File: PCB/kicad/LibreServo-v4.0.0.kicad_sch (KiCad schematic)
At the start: 105 parts, among them J1 SLOT, J2 SLOT, J3 FFC-5, J4 FFC-5, J5 HEADER_4_1.27_0.3, J6 JST_PH-4_HOLEB, J7 JST_PH-4_HOLEB, M1 M1, M2 MOSFET_N+P, M3 MOSFET_N+P, M4 FAN3227/4, M5 FAN3227/4, U1 M0G3518QRHBRQ1, U10 AEAT-8800, U2 MPM3610, U3 AP2112, U4 ACS711, U5 ADM2587E, U6 ADM3055E, U7 OPTIGA_TRUST_M, Y1 OSCILATOR

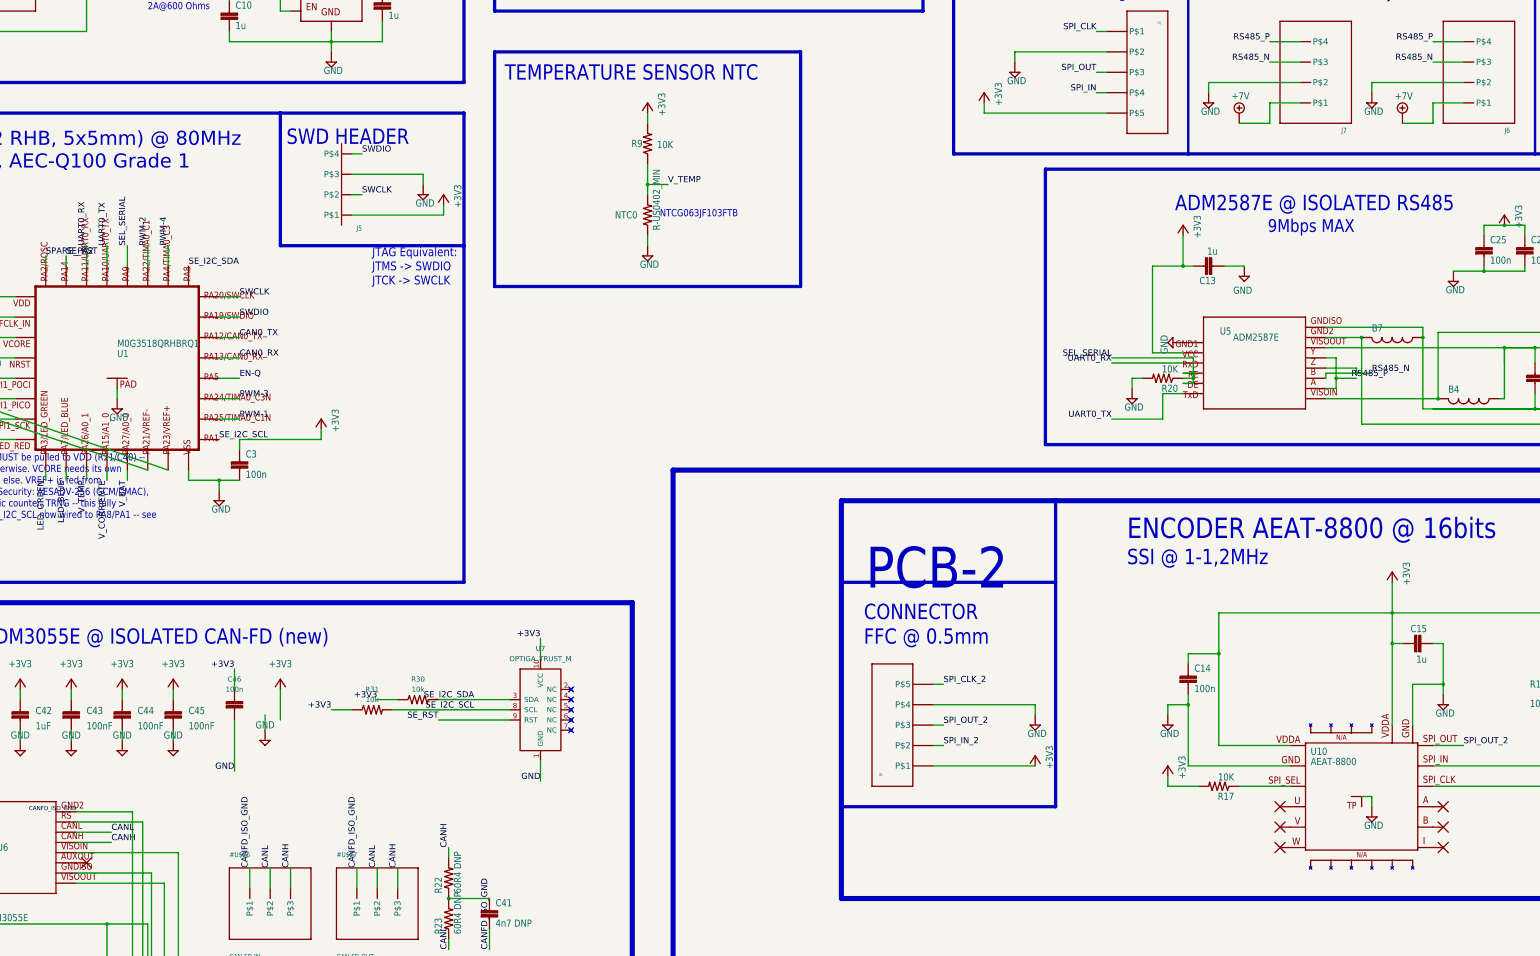
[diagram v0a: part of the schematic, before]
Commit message: fix(sch): add PWR_FLAG on 10 legitimately-external/isolated supply nets
Places power:PWR_FLAG instances on the nets ERC correctly reports as
"power_pin_not_driven" because nothing in the schematic supplies them
from a real driven output pin -- they're genuinely externally-sourced
or internally isoPower-generated:

  - U5 (ADM2587E) GNDISO / GND2 / VISOIN / VISOOUT -- isolated-side
    supply generated by the part's own integrated isoPower converter,
    not modeled as a driving pin on the symbol.
  - U6 (ADM3055E) the same 4 isolated-side nets, mirroring U5.
  - Board +7V and GND, sourced from the external battery/motor
    connector (J6/J7), which this schematic correctly can't infer as
    "driven" without an explicit flag.

Also registers the "power" library in the project's own sym-lib-table
(previously only resolvable via the user's global KiCad config) and
adds the ki_keywords property that was missing from the first,
incomplete embed -- both were needed to clear a lib_symbol_mismatch
ERC error that appeared on all 10 instances until fixed.

power_pin_not_driven: 17 -> 7; ERC errors: 21 -> 11. The still-open 6
U4 (ACS711 current sensor) pin_to_pin findings are a separate, known
false positive from the ACS711 symbol's power-carrying IP+/IP- pins
being typed "bidirectional" rather than "passive"/"power" -- tracked
for a waiver, not a wiring fix.

Co-Authored-By: Claude Sonnet 5 <noreply@anthropic.com>
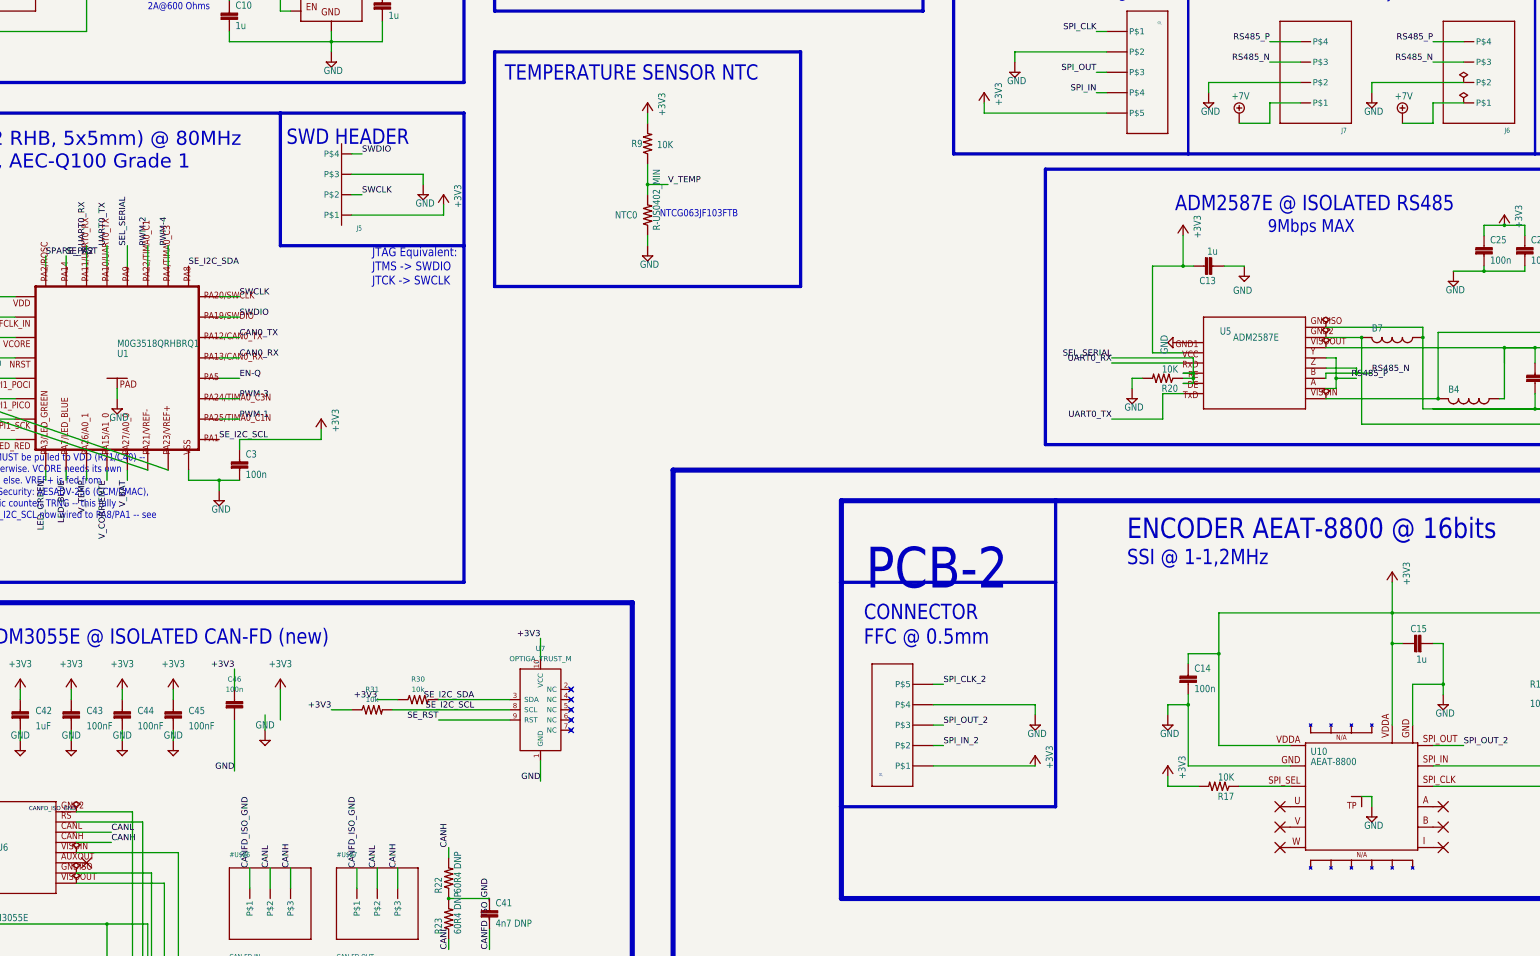
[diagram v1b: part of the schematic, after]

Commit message: fix(sch): resolve power-tree ERC errors (AGND, VCORE, VMOT mislabel, PWR_FLAGs)
Multiple independent fixes, each verified via kicad-cli sch erc +
sch export netlist before combining:

- U2 (MPM3610 buck) AGND (P\$3) was a genuinely isolated 2-pin island
  (only tied to feedback resistor R1, never reaching board GND). Added
  a GND symbol at the same point -- the datasheet-preferred treatment
  (a dedicated low-noise star-ground point for the feedback divider,
  distinct from the switching PGND) is a PCB-layout copper concern,
  not a schematic connectivity one; MPM3610 datasheet not locally
  available to verify further, tracked as a new TODO item.
- U1 VCORE (pin 32): added a PWR_FLAG. This is the MCU's internally-
  regulated core rail (decoupling-cap-only per TI's usual guidance,
  not an externally driven supply), a standard, expected ERC pattern.
- U2's true P\$16 (IN) pin was misidentified in an earlier pass as one
  of three PGND-group pins that happen to share IN's old visual
  column; corrected the PWR_FLAG placed on it to the pin's real
  local coordinate (7.62, 22.86, angle 270), resolving both its own
  violation and a pin_to_pin collision the wrong placement had
  introduced against the GND PWR_FLAG.
- U3 (AP2112 LDO) input (pin 1, fed from U2's regulated output through
  ferrite B2): added a PWR_FLAG. U2's VOUT pin is typed generic
  "output" rather than "power_out" in the EAGLE-imported symbol,
  so ERC doesn't credit it as a driver of downstream stages -- a
  symbol-library limitation, not a wiring defect.
- Found and fixed a real labeling bug: two power-symbol instances
  (#P+5, #P+6) used the "+5V" symbol type (which asserts membership
  in the global +5V net via its pin name) while their Value property
  had been hand-edited to display "Vmot" -- changing Value text does
  NOT change a KiCad power symbol's underlying electrical net tie, so
  these were silently still part of a nonexistent "+5V" net rather
  than the real VMOT rail. Replaced both wi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
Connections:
- net GND: now also R1.1, U2.P$3 (P$3_AGND)
- net Vmot renamed VMOT
